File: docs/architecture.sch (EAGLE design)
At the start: 22 parts, among them J3 40V

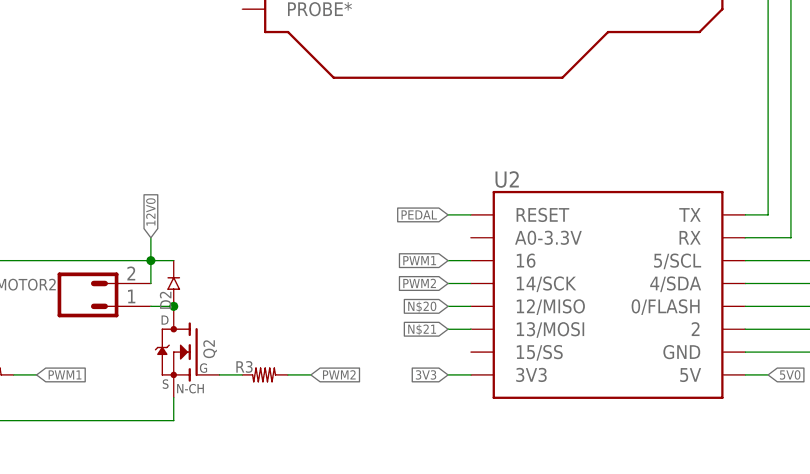
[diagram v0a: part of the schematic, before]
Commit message: added counter_in to esp added all the v2 freecad files
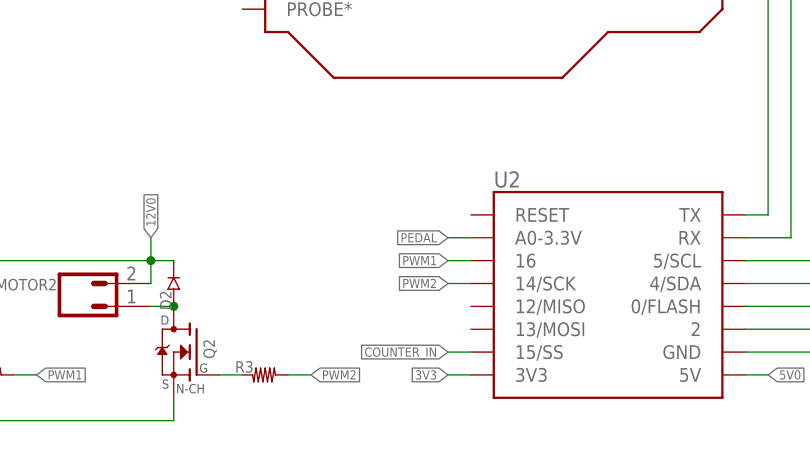
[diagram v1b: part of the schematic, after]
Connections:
- removed net N$20: U2.12/MISO
- removed net N$21: U2.13/MOSI
- new net COUNTER_IN: U2.15/SS
- net PEDAL: now also U2.A0-3.3V; no longer U2.RESET
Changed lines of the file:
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@@
 </segment>
 <segment>
-<pinref part="U2" gate="G$1" pin="RESET"/>
-<wire x1="106.68" y1="76.2" x2="104.14" y2="76.2" width="0.1524" layer="91"/>
-<label x="104.14" y="76.2" size="1.016" layer="95" rot="R180" xref="yes"/>
+<pinref part="U2" gate="G$1" pin="A0-3.3V"/>
+<wire x1="106.68" y1="73.66" x2="104.14" y2="73.66" width="0.1524" layer="91"/>
+<label x="104.14" y="73.66" size="1.016" layer="95" rot="R180" xref="yes"/>
 </segment>
 </net>
@@
 <wire x1="86.36" y1="58.42" x2="88.9" y2="58.42" width="0.1524" layer="91"/>
 <label x="88.9" y="58.42" size="1.016" layer="95" xref="yes"/>
-</segment>
-</net>
-<net name="N$20" class="0">
-<segment>
-<pinref part="U2" gate="G$1" pin="12/MISO"/>
-<wire x1="106.68" y1="66.04" x2="104.14" y2="66.04" width="0.1524" layer="91"/>
-<label x="104.14" y="66.04" size="1.016" layer="95" rot="R180" xref="yes"/>
-</segment>
-</net>
-<net name="N$21" class="0">
-<segment>
-<pinref part="U2" gate="G$1" pin="13/MOSI"/>
-<wire x1="106.68" y1="63.5" x2="104.14" y2="63.5" width="0.1524" layer="91"/>
-<label x="104.14" y="63.5" size="1.016" layer="95" rot="R180" xref="yes"/>
 </segment>
 </net>
@@
 </segment>
 </net>
+<net name="COUNTER_IN" class="0">
+<segment>
+<pinref part="U2" gate="G$1" pin="15/SS"/>
+<wire x1="106.68" y1="60.96" x2="104.14" y2="60.96" width="0.1524" layer="91"/>
+<label x="104.14" y="60.96" size="1.016" layer="95" rot="R180" xref="yes"/>
+</segment>
+</net>

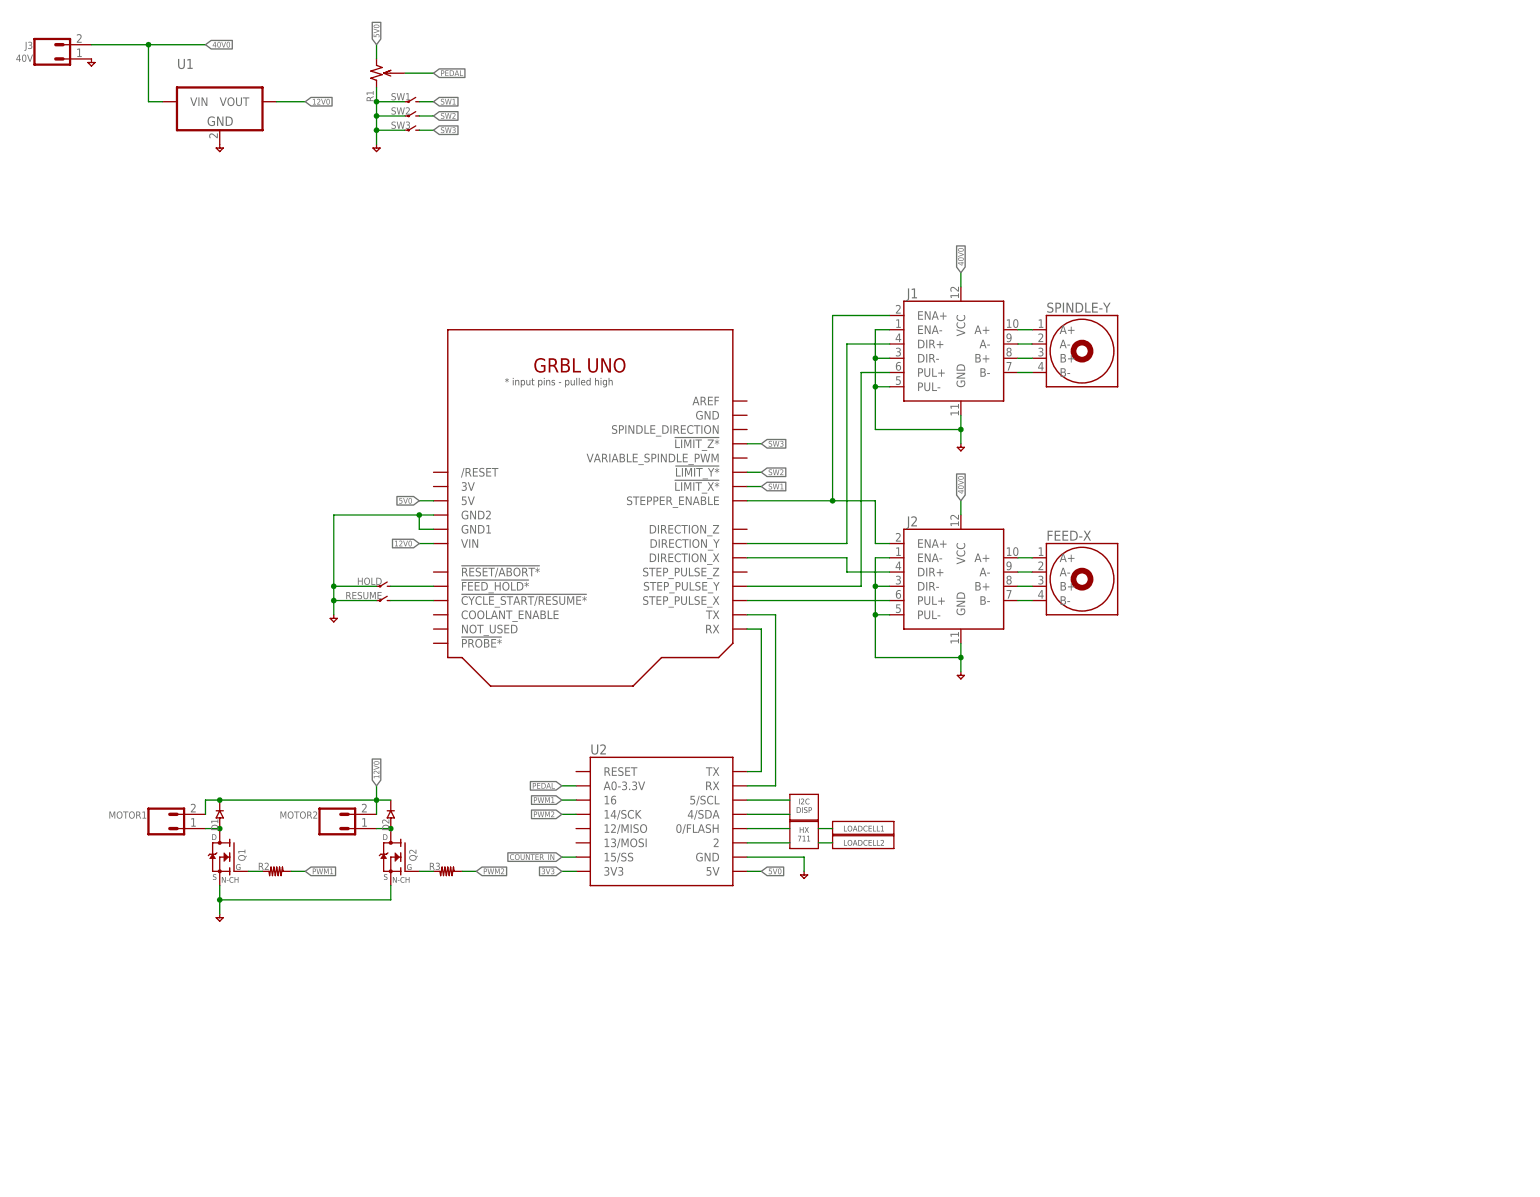
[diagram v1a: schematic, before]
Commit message: initial add for babysteps and JGY370 files updated the architecture schematic
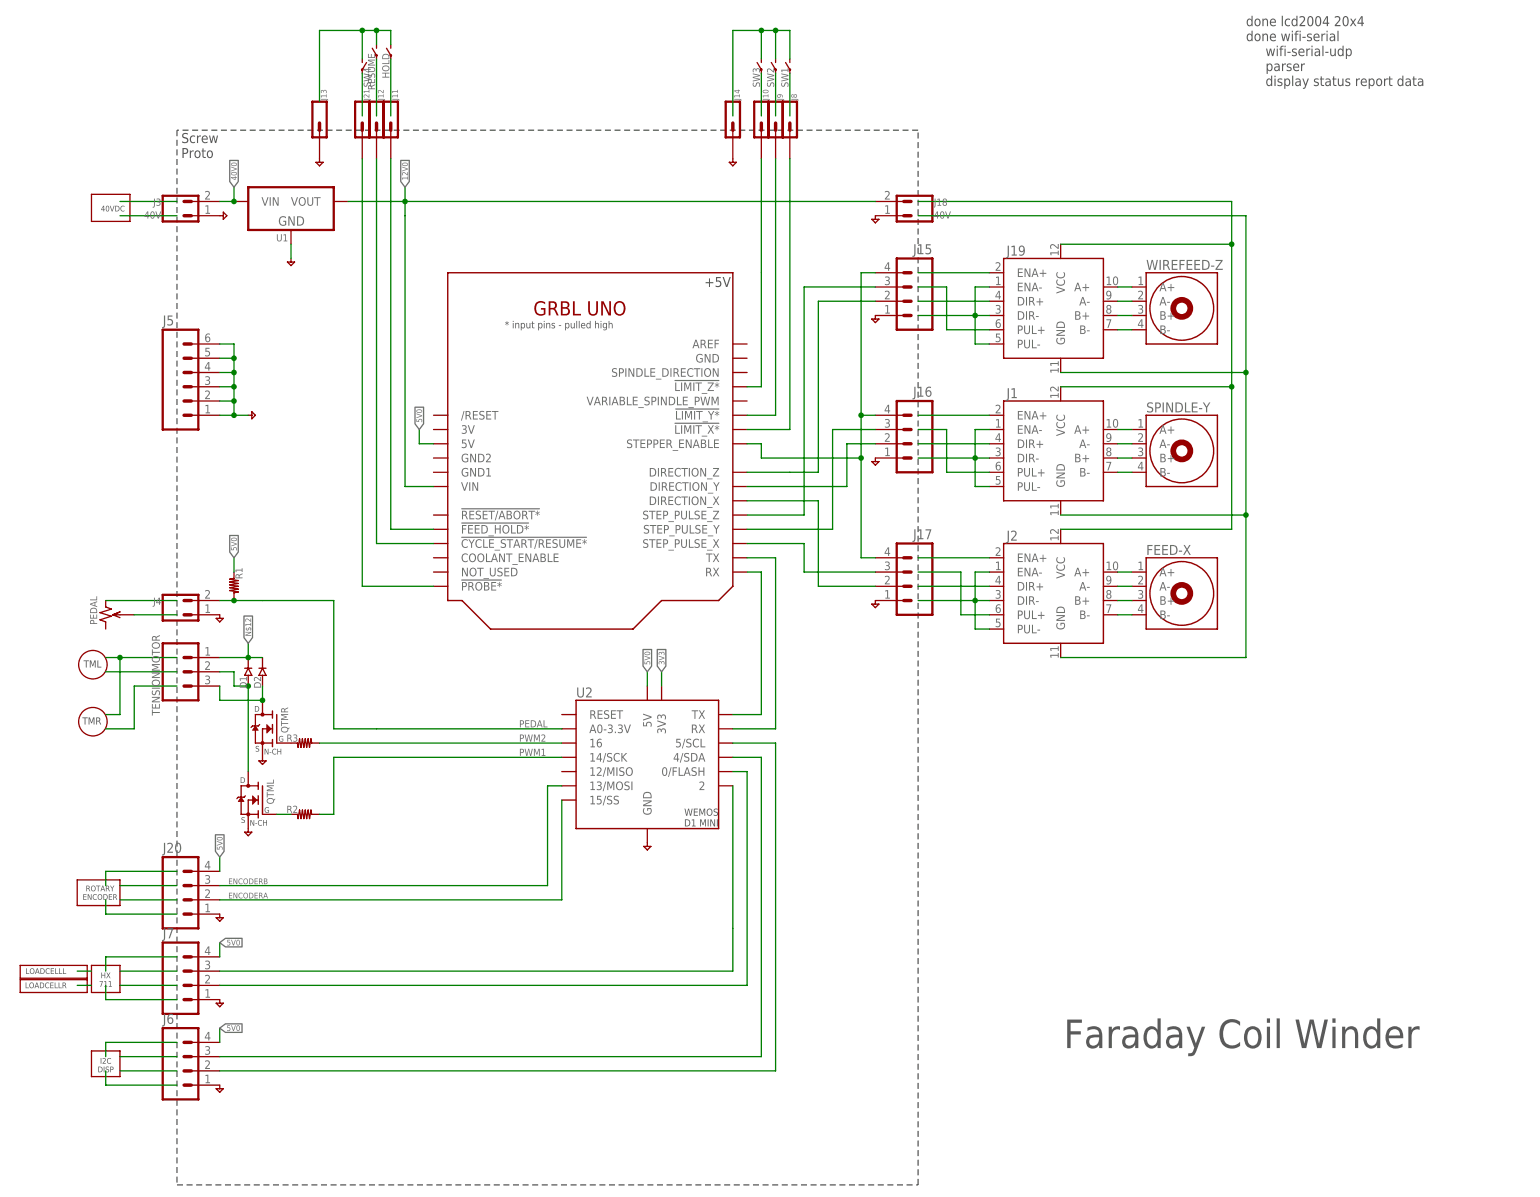
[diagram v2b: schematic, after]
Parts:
- removed MOTOR1, MOTOR2: (no value), holla:CONN-02-3.81MM-PLUGIN-SCREW
- removed Q1, Q2: (no value), holla:FET-NCH-TO252
- added J10, J11, J12, J13, J14, J21, J8, J9: (no value), holla:CONN-01
- added J15, J16, J17, J20, J6, J7: (no value), holla:CONN-04-.100-VERT-HEADER
- added J18: 40V, holla:CONN-02-3.81MM-PLUGIN-SCREW
- added J19: (no value), holla:MOTOR-STEPPER-DRIVER-SINGLE
- added J4: (no value), holla:CONN-02-.100-VERT-HEADER
- added J5: (no value), holla:CONN-06-.100-VERT-HEADER
- added PEDAL: (no value), holla:POTENTIOMETER
- added QTML, QTMR: (no value), holla:FET-NCH-TO252
- added SW4: (no value), holla:SWITCH-PANEL-SPST
- added TENSIONMOTOR: (no value), holla:CONN-03-.100
- added WIREFEED-Z: (no value), holla:MOTOR-STEPPER-BIPOLAR
- R1: device holla:POTENTIOMETER -> holla:R-0805
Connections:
- removed net COUNTER_IN: U2.15/SS
- removed net N$12: J1.DIR+, U$1.DIRECTION_Y
- removed net N$9: J2.PUL+, U$1.STEP_PULSE_X
- removed net SW1: SW1.2, U$1.!LIMIT_X*
- removed net SW2: SW2.2, U$1.!LIMIT_Y*
- removed net SW3: SW3.2, U$1.!LIMIT_Z*
- new net ENCODERA: J20.2, U2.15/SS
- new net ENCODERB: J20.3, U2.13/MOSI
- new net N$20: PEDAL.2
- new net N$21: PEDAL.W
- new net N$33: J10.1, U$1.!LIMIT_Z*
- new net N$34: J9.1, U$1.!LIMIT_Y*
- new net N$35: SW3.1
- new net N$36: SW2.1
- new net N$37: SW1.1
- new net N$38: SW1.2, SW2.2, SW3.2
- new net N$39: J8.1, U$1.!LIMIT_X*
- new net N$48: J11.1, U$1.!FEED_HOLD*
- new net N$49: J12.1, U$1.!CYCLE_START/RESUME*
- new net N$50: HOLD.2, RESUME.2, SW4.2
- new net N$51: J15.2, U$1.DIRECTION_Z
- new net N$52: J15.3, U$1.STEP_PULSE_Z
- new net N$53: J2.DIR+
- new net N$54: J16.2, U$1.DIRECTION_Y
- new net N$55: J16.3, U$1.STEP_PULSE_Y
- new net N$56: J17.3, U$1.STEP_PULSE_X
- new net N$57: J2.PUL+
- new net N$58: J1.ENA+
- new net N$59: J1.DIR+
- new net N$60: J19.A+, WIREFEED-Z.A+
- new net N$61: J19.A-, WIREFEED-Z.A-
- new net N$62: J19.B+, WIREFEED-Z.B+
- new net N$63: J19.B-, WIREFEED-Z.B-
- new net N$64: J19.ENA+
- new net N$65: J19.DIR+
- new net N$66: J19.PUL+
- new net N$67: J19.DIR-, J19.ENA-, J19.PUL-
- new net N$68: J1.DIR-, J1.ENA-, J1.PUL-
- new net N$69: J2.DIR-, J2.ENA-, J2.PUL-
- new net N$70: J1.VCC, J19.VCC, J2.VCC
- new net N$71: J1.GND, J19.GND
- new net N$74: J2.GND
- new net N$79: J21.1, U$1.!PROBE*
- new net N$80: SW4.1
- new net N$83: J15.4, J16.4, J17.4, U$1.STEPPER_ENABLE
- net 12V0: now also J18.2; no longer D1.C, D2.C, MOTOR1.2, MOTOR2.2
- net 40V0: now also D1.C, D2.C, TENSIONMOTOR.1; no longer J1.VCC, J2.VCC
- net 5V0: now also J20.4, J6.4, J7.4, R1.1; no longer R1.2
- net GND: now also J13.1, J14.1, J15.1, J16.1, J17.1, J18.1, J20.1, J4.1, J5.1, J5.2, J5.3, J5.4, J5.5, J5.6, J6.1, J7.1, QTML.S, QTMR.S; no longer HOLD.1, J1.DIR-, J1.ENA-, J1.GND, J1.PUL-, J2.DIR-, J2.ENA-, J2.GND, J2.PUL-, Q1.S, Q2.S, R1.1, RESUME.1, SW1.1, SW2.1, SW3.1, U$1.GND1, U$1.GND2
- net N$10: no longer U$1.STEP_PULSE_Y
- net N$11: now also J17.2; no longer J2.DIR+
- net N$13: no longer J1.ENA+, U$1.STEPPER_ENABLE
- net N$16: now also RESUME.1; no longer HOLD.2, U$1.!FEED_HOLD*
- net N$17: now also HOLD.1; no longer RESUME.2, U$1.!CYCLE_START/RESUME*
- net N$18: now also J6.2
- net N$19: now also J6.3
- net N$22: now also J7.2
- net N$23: now also J7.3
- net N$26: now also QTML.D, TENSIONMOTOR.2; no longer MOTOR1.1, Q1.D
- net N$27: now also QTMR.D, TENSIONMOTOR.3; no longer MOTOR2.1, Q2.D
- net N$28: now also QTMR.G; no longer Q2.G
- net N$29: now also QTML.G; no longer Q1.G
- net PEDAL: now also J4.2, R1.2; no longer R1.W
- net PWM1: now also U2.14/SCK; no longer U2.16
- net PWM2: now also U2.16; no longer U2.14/SCK
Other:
- note added: "+5V"
- note added: "40VDC"
- note added: "Faraday Coil Winder"
- note added: "LOADCELLL"
- note added: "LOADCELLR"
- note added: "ROTARY ENCODER"
- note added: "Screw Proto"
- note added: "TML"
- note added: "TMR"
- note added: "done lcd2004 20x4 done wifi-serial wifi-serial-udp parser display status report data"
- note removed: "LOADCELL1"
- note removed: "LOADCELL2"
- moved on the sheet: D1, D2, FEED-X, HOLD, J1, J2, J3, R2, R3, RESUME, SPINDLE-Y, SW1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

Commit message: added block diagram
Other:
- note added: "Faraday Gateway"
- note added: "GRBL"
- note added: "HTTP"
- note added: "I2C"
- note added: "LCD Display 20x4"
- note added: "Serial"
- note added: "TCP"
- note added: "WS"
- note added: "browserDRO"
- note added: "done lcd2004 20x4 done wifi-serial-http-tcp wifi-serial-http-websockets parser display status report data"
- note added: "faradayConsole.py"
- note removed: "done lcd2004 20x4 done wifi-serial wifi-serial-udp parser display status report data"
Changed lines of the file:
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@@
 ENCODER</text>
 <text x="226.06" y="210.82" size="1.778" layer="97" align="top-left">done lcd2004 20x4
-done wifi-serial
-     wifi-serial-udp
+done wifi-serial-http-tcp
+     wifi-serial-http-websockets
      parser
      display status report data
 </text>
+<wire x1="180.34" y1="58.42" x2="208.28" y2="58.42" width="0.1524" layer="97"/>
+<wire x1="208.28" y1="58.42" x2="208.28" y2="55.88" width="0.1524" layer="97"/>
+<wire x1="208.28" y1="55.88" x2="208.28" y2="53.34" width="0.1524" layer="97"/>
+<wire x1="208.28" y1="53.34" x2="180.34" y2="53.34" width="0.1524" layer="97"/>
+<wire x1="180.34" y1="53.34" x2="180.34" y2="58.42" width="0.1524" layer="97"/>
+<text x="194.31" y="55.88" size="1.778" layer="97" align="center">faradayConsole.py</text>
+<wire x1="180.34" y1="50.8" x2="208.28" y2="50.8" width="0.1524" layer="97"/>
+<wire x1="208.28" y1="50.8" x2="208.28" y2="49.53" width="0.1524" layer="97"/>
+<wire x1="208.28" y1="49.53" x2="208.28" y2="46.99" width="0.1524" layer="97"/>
+<wire x1="208.28" y1="46.99" x2="208.28" y2="45.72" width="0.1524" layer="97"/>
+<wire x1="208.28" y1="45.72" x2="180.34" y2="45.72" width="0.1524" layer="97"/>
+<wire x1="180.34" y1="45.72" x2="180.34" y2="50.8" width="0.1524" layer="97"/>
+<text x="194.31" y="48.26" size="1.778" layer="97" align="center">browserDRO</text>
+<wire x1="218.44" y1="58.42" x2="231.14" y2="58.42" width="0.1524" layer="97"/>
+<wire x1="231.14" y1="58.42" x2="246.38" y2="58.42" width="0.1524" layer="97"/>
+<wire x1="246.38" y1="58.42" x2="246.38" y2="53.34" width="0.1524" layer="97"/>
+<wire x1="246.38" y1="53.34" x2="246.38" y2="45.72" width="0.1524" layer="97"/>
+<wire x1="246.38" y1="45.72" x2="218.44" y2="45.72" width="0.1524" layer="97"/>
+<wire x1="218.44" y1="45.72" x2="218.44" y2="46.99" width="0.1524" layer="97"/>
+<text x="232.664" y="52.07" size="1.778" layer="97" align="center">Faraday
+Gateway</text>
+<wire x1="218.44" y1="46.99" x2="218.44" y2="49.53" width="0.1524" layer="97"/>
+<wire x1="218.44" y1="49.53" x2="218.44" y2="55.88" width="0.1524" layer="97"/>
+<wire x1="218.44" y1="55.88" x2="218.44" y2="58.42" width="0.1524" layer="97"/>
+<wire x1="208.28" y1="55.88" x2="218.44" y2="55.88" width="0.1524" layer="97"/>
+<wire x1="208.28" y1="49.53" x2="218.44" y2="49.53" width="0.1524" layer="97"/>
+<wire x1="208.28" y1="46.99" x2="218.44" y2="46.99" width="0.1524" layer="97"/>
+<text x="214.122" y="56.134" size="1.778" layer="97" align="bottom-center">TCP</text>
+<text x="213.868" y="49.784" size="1.778" layer="97" align="bottom-center">HTTP</text>
+<text x="213.868" y="47.244" size="1.778" layer="97" align="bottom-center">WS</text>
+<wire x1="218.44" y1="68.58" x2="246.38" y2="68.58" width="0.1524" layer="97"/>
+<wire x1="246.38" y1="68.58" x2="246.38" y2="66.04" width="0.1524" layer="97"/>
+<wire x1="246.38" y1="63.5" x2="231.14" y2="63.5" width="0.1524" layer="97"/>
+<wire x1="231.14" y1="63.5" x2="218.44" y2="63.5" width="0.1524" layer="97"/>
+<wire x1="218.44" y1="63.5" x2="218.44" y2="68.58" width="0.1524" layer="97"/>
+<text x="232.41" y="66.04" size="1.778" layer="97" align="center">LCD Display 20x4</text>
+<wire x1="246.38" y1="63.5" x2="246.38" y2="66.04" width="0.1524" layer="97"/>
+<wire x1="231.14" y1="63.5" x2="231.14" y2="58.42" width="0.1524" layer="97"/>
+<wire x1="256.54" y1="55.88" x2="266.7" y2="55.88" width="0.1524" layer="97"/>
+<wire x1="266.7" y1="50.8" x2="261.62" y2="50.8" width="0.1524" layer="97"/>
+<wire x1="261.62" y1="50.8" x2="256.54" y2="50.8" width="0.1524" layer="97"/>
+<wire x1="256.54" y1="50.8" x2="256.54" y2="53.34" width="0.1524" layer="97"/>
+<text x="262.128" y="53.594" size="1.778" layer="97" align="center">GRBL</text>
+<wire x1="256.54" y1="53.34" x2="256.54" y2="55.88" width="0.1524" layer="97"/>
+<wire x1="266.7" y1="55.88" x2="266.7" y2="50.8" width="0.1524" layer="97"/>
+<wire x1="246.38" y1="53.34" x2="256.54" y2="53.34" width="0.1524" layer="97"/>
+<text x="247.65" y="53.594" size="1.778" layer="97">Serial</text>
+<text x="230.886" y="58.928" size="1.778" layer="97" rot="R90">I2C</text>
 </plain>
 <instances>

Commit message: initial commit for src and docs, tweaked schematic
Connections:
- new net N$9: U$1.COOLANT_ENABLE, U2.12/MISO
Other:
- note added: "done lcd2004 20x4 done wifi-serial-http-tcp wifi-serial-http-websockets parser display status report data load cell query tension driver grbl status parser rotary encoder interrupts comment parser"
- note removed: "done lcd2004 20x4 done wifi-serial-http-tcp wifi-serial-http-websockets parser display status report data"
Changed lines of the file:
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@@
      parser
      display status report data
+     load cell query
+     tension driver
+     grbl status parser
+     rotary encoder interrupts
+     comment parser
 </text>
 <wire x1="180.34" y1="58.42" x2="208.28" y2="58.42" width="0.1524" layer="97"/>
@@
 </segment>
 </net>
+<net name="N$9" class="0">
+<segment>
+<pinref part="U$1" gate="G$1" pin="COOLANT_ENABLE"/>
+<wire x1="81.28" y1="114.3" x2="71.12" y2="114.3" width="0.1524" layer="91"/>
+<wire x1="71.12" y1="114.3" x2="71.12" y2="76.2" width="0.1524" layer="91"/>
+<pinref part="U2" gate="G$1" pin="12/MISO"/>
+<wire x1="71.12" y1="76.2" x2="104.14" y2="76.2" width="0.1524" layer="91"/>
+</segment>
+</net>
